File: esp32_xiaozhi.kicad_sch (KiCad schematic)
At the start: 5 parts

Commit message: Update schematics, PCB, and project files
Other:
- sheet esp32_C6 ports: added none; removed EN, IO_12, IO_13
- sheet max98357a ports: added none; removed GAIN, SD
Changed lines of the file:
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@@
-	(wire
-		(pts
-			(xy 168.91 107.95) (xy 177.8 107.95)
-		)
-		(stroke
-			(width 0)
-			(type default)
-		)
-	)
 	(wire
 		(pts
@@
 	(wire
 		(pts
-			(xy 220.98 105.41) (xy 232.41 105.41)
-		)
-		(stroke
-			(width 0)
-			(type default)
-		)
-	)
-	(wire
-		(pts
 			(xy 204.47 193.04) (xy 210.82 193.04)
 		)
@@
 		(pts
 			(xy 299.085 71.12) (xy 304.8 71.12)
-		)
-		(stroke
-			(width 0)
-			(type default)
-		)
-	)
-	(wire
-		(pts
-			(xy 220.98 107.95) (xy 237.49 107.95)
 		)
 		(stroke
@@
 		)
 	)
-	(label "IO_12"
-		(at 232.41 105.41 0)
-		(effects
-			(font
-				(size 1.27 1.27)
-			)
-			(justify left bottom)
-		)
-	)
 	(label "IO_11"
 		(at 245.11 72.39 180)
@@
 		)
 	)
-	(label "IO_13"
-		(at 237.49 107.95 0)
-		(effects
-			(font
-				(size 1.27 1.27)
-			)
-			(justify left bottom)
-		)
-	)
 	(label "OE"
 		(at 238.76 59.69 0)
@@
 			)
 			(justify right bottom)
-		)
-	)
-	(label "EN"
-		(at 168.91 107.95 0)
-		(effects
-			(font
-				(size 1.27 1.27)
-			)
-			(justify left bottom)
 		)
 	)
@@
 			)
 		)
-		(pin "GAIN" input
-			(at 74.93 143.51 0)
-			(effects
-				(font
-					(size 1.27 1.27)
-				)
-				(justify right)
-			)
-		)
 		(pin "LRC" input
 			(at 74.93 124.46 0)
-			(effects
-				(font
-					(size 1.27 1.27)
-				)
-				(justify right)
-			)
-		)
-		(pin "SD" input
-			(at 74.93 132.08 0)
 			(effects
 				(font
@@
 			)
 		)
-		(pin "EN" input
-			(at 177.8 107.95 180)
-			(effects
-				(font
-					(size 1.27 1.27)
-				)
-				(justify left)
-			)
-		)
 		(pin "IO_0" input
 			(at 177.8 111.76 180)
@@
 			)
 		)
-		(pin "IO_12" input
-			(at 220.98 105.41 0)
-			(effects
-				(font
-					(size 1.27 1.27)
-				)
-				(justify right)
-			)
-		)
-		(pin "IO_13" input
-			(at 220.98 107.95 0)
-			(effects
-				(font
-					(size 1.27 1.27)
-				)
-				(justify right)
-			)
-		)

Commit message: Add PWR_FLAG symbols to all schematic sheets to fix power_pin_not_driven ERC errors
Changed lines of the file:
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@@
 	)
 	(embedded_fonts no)
+	(symbol
+		(lib_id "power:PWR_FLAG")
+		(at 105.41 195.0 0)
+		(unit 1)
+		(body_style 1)
+		(exclude_from_sim no)
+		(in_bom no)
+		(on_board yes)
+		(in_pos_files no)
+		(dnp no)
+		(property "Reference" "#FLG007"
+			(at 105.41 190.0 0)
+			(hide yes)
+			(show_name no)
+			(do_not_autoplace no)
+			(effects
+				(font
+					(size 1.27 1.27)
+				)
+			)
+		)
+		(property "Value" "PWR_FLAG"
+			(at 105.41 200.0 0)
+			(hide yes)
+			(show_name no)
+			(do_not_autoplace no)
+			(effects
+				(font
+					(size 1.27 1.27)
+				)
+			)
+		)
+		(pin "1"
+			(uuid "a1b2c3d4-e5f6-7890-abcd-ef1234567890-pin1")
+		)
+		(instances
+			(project "esp32_xiaozhi"
+				(path "/cae338e8-f342-43cb-b99a-a0486629133c"
+					(reference "#FLG007")
+					(unit 1)
+				)
+			)
+		)
+	)
 )

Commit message: Revert PWR_FLAG additions - remove '??' squares from schematics
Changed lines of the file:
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@@
 	)
 	(embedded_fonts no)
-	(symbol
-		(lib_id "power:PWR_FLAG")
-		(at 105.41 195.0 0)
-		(unit 1)
-		(body_style 1)
-		(exclude_from_sim no)
-		(in_bom no)
-		(on_board yes)
-		(in_pos_files no)
-		(dnp no)
-		(property "Reference" "#FLG007"
-			(at 105.41 190.0 0)
-			(hide yes)
-			(show_name no)
-			(do_not_autoplace no)
-			(effects
-				(font
-					(size 1.27 1.27)
-				)
-			)
-		)
-		(property "Value" "PWR_FLAG"
-			(at 105.41 200.0 0)
-			(hide yes)
-			(show_name no)
-			(do_not_autoplace no)
-			(effects
-				(font
-					(size 1.27 1.27)
-				)
-			)
-		)
-		(pin "1"
-			(uuid "a1b2c3d4-e5f6-7890-abcd-ef1234567890-pin1")
-		)
-		(instances
-			(project "esp32_xiaozhi"
-				(path "/cae338e8-f342-43cb-b99a-a0486629133c"
-					(reference "#FLG007")
-					(unit 1)
-				)
-			)
-		)
-	)
 )

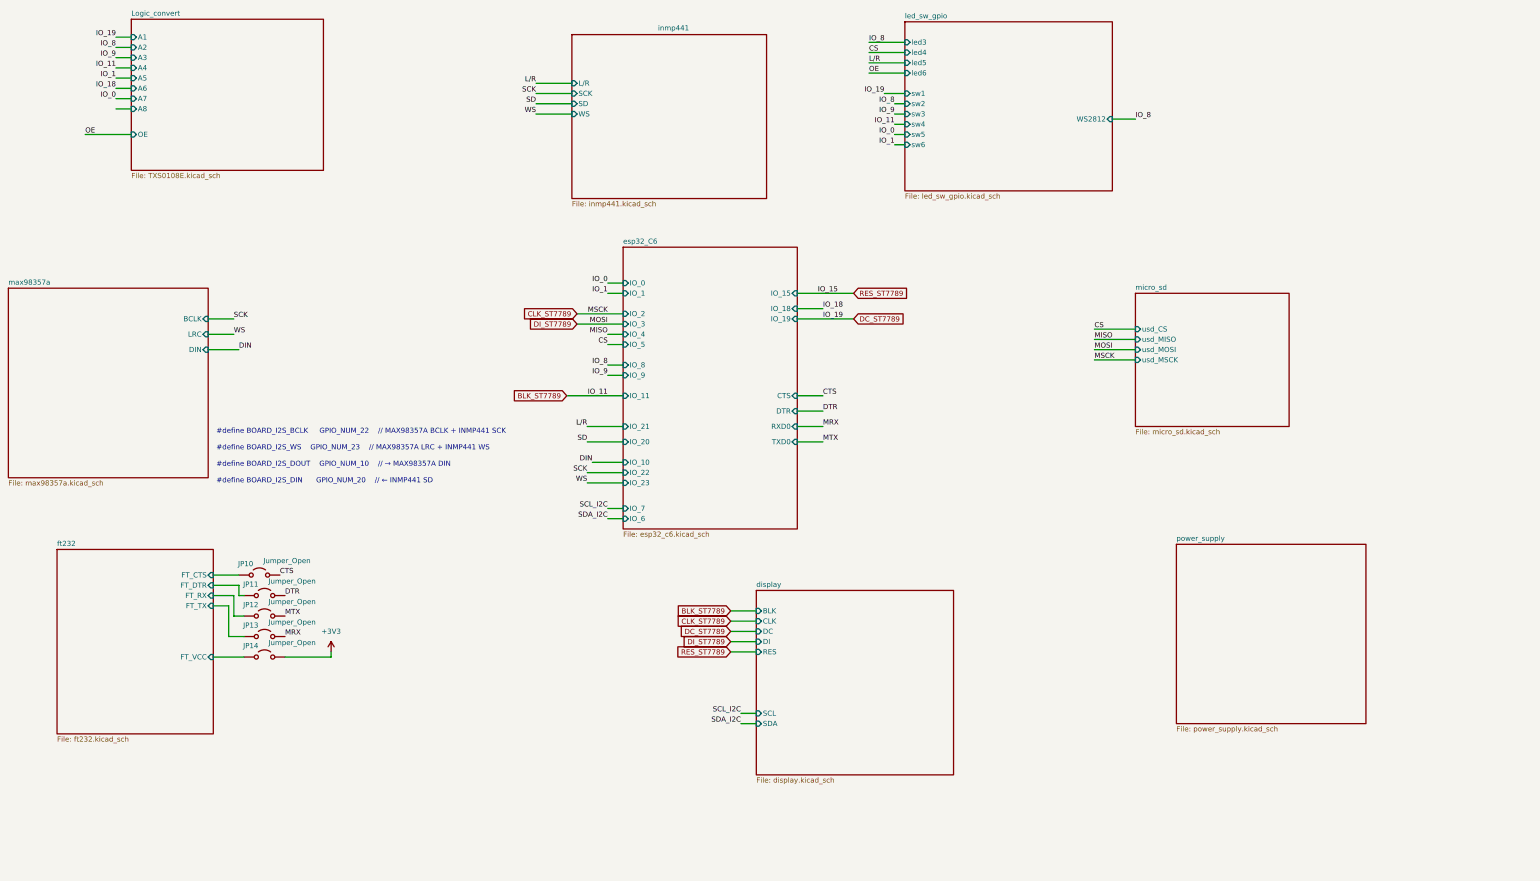
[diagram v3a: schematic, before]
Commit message: Actualización de esquema y PCB del proyecto ESP32C6 Xiaozhi
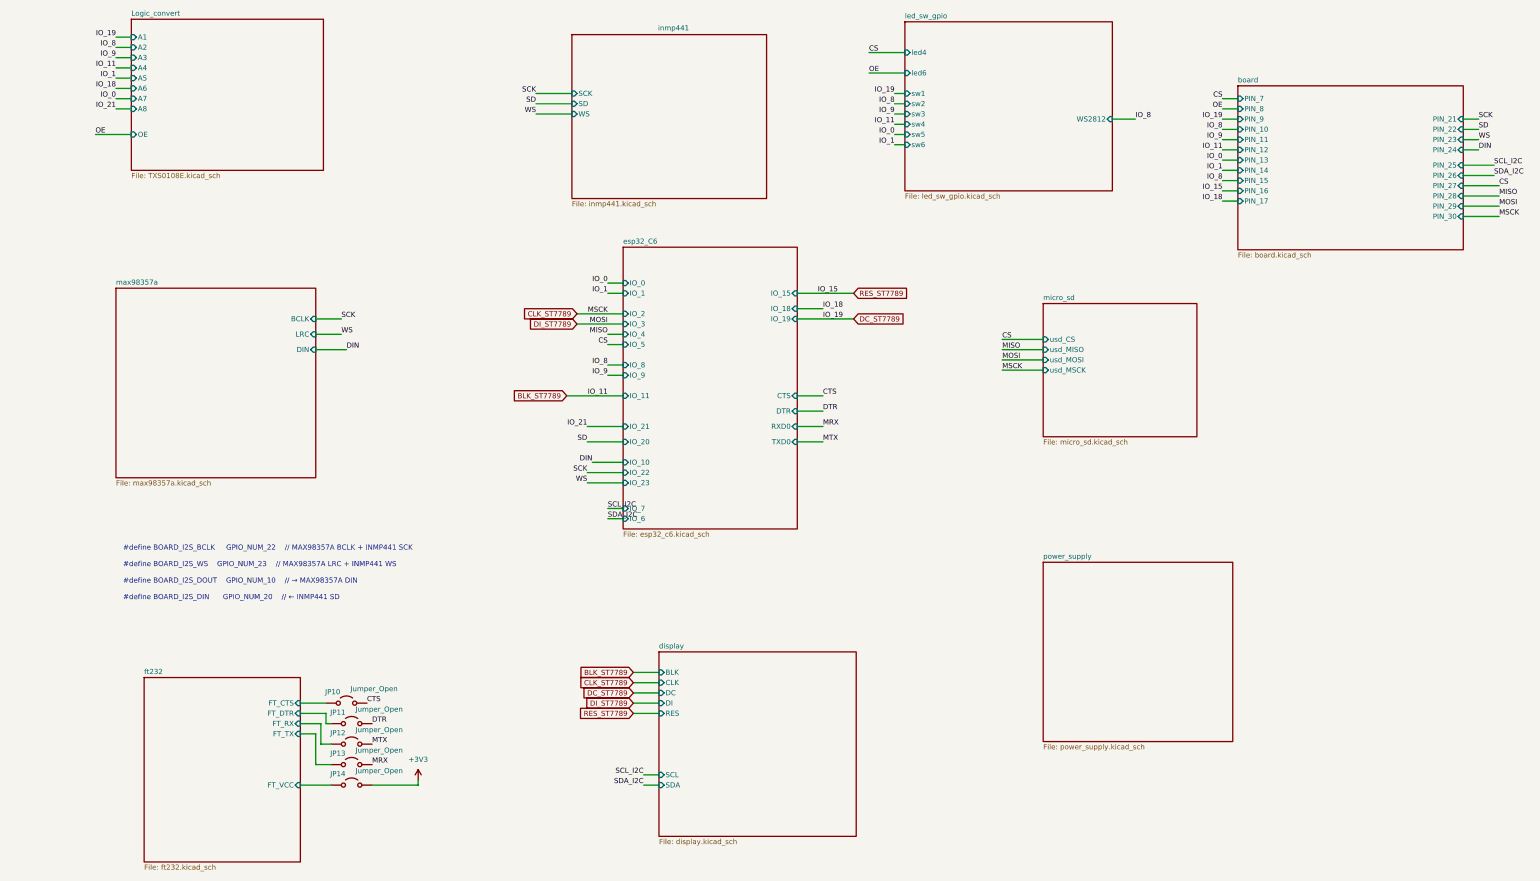
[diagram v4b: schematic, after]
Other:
- added sheet board (board.kicad_sch)
- sheet inmp441 ports: added none; removed L/R
- sheet led_sw_gpio ports: added none; removed led3, led5
- moved on the sheet: JP10, JP11, JP12, JP13, JP14

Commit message: Actualizaciones para versión single ESP32C6
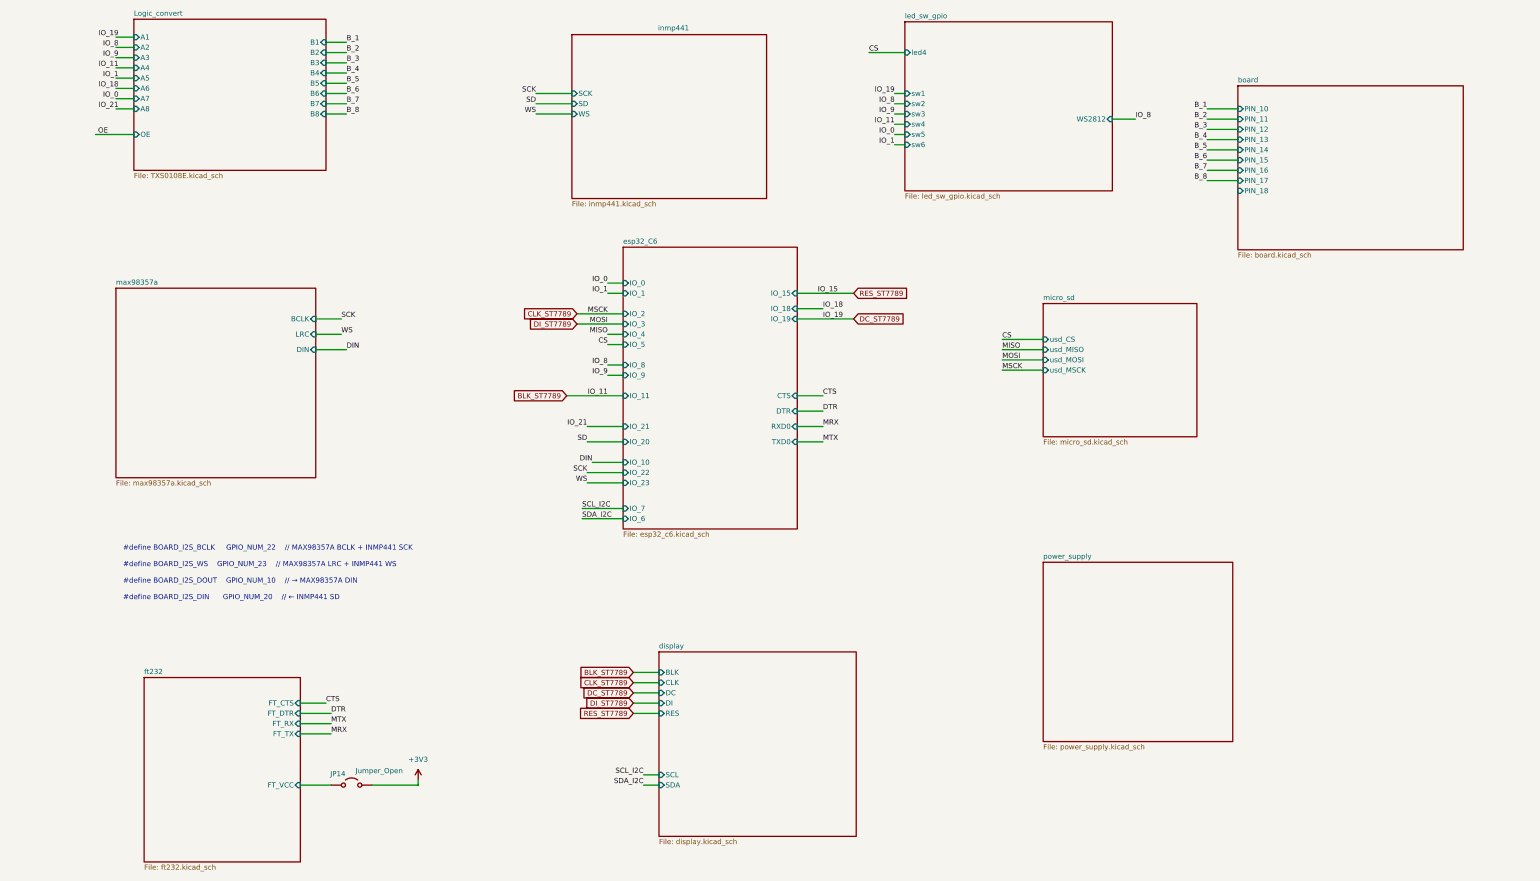
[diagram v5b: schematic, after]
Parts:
- removed JP10, JP11, JP12, JP13: Jumper_Open, Jumper:SolderJumper-2_P1.3mm_Open_RoundedPad1.0x1.5mm, symbol Jumper:Jumper_2_Open
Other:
- sheet Logic_convert ports: added B1, B2, B3, B4, B5, B6, B7, B8; removed none
- sheet board ports: added PIN_18; removed PIN_21, PIN_22, PIN_23, PIN_24, PIN_25, PIN_26, PIN_27, PIN_28, PIN_29, PIN_30, PIN_7, PIN_8, PIN_9
- sheet led_sw_gpio ports: added none; removed led6

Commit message: SCH: Update main schematic
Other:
- removed sheet board

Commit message: Actualización de esquemas y PCB con datos LCSC y librerías JLC
- Añade propiedades LCSC a los símbolos de las hojas de esquema
- Actualiza las hojas TXS0108E, display, esp32_c6, ft232, inmp441,
  led_sw_gpio, max98357a, micro_sd, power_supply y el esquema raíz
- Reorganiza el PCB (footprints, jumpers y nets) y actualiza el proyecto
- Incluye las librerías locales JLCImport (símbolos, huellas y modelos 3D)
  y las entradas correspondientes en fp-lib-table y sym-lib-table
- Añade la documentación técnica en docs/ y el archivo de posiciones
  esp32_xiaozhi-all.pos
- Elimina los ZIP generados gebers.zip y production.zip
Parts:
- JP14: now left out of the parts list
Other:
- sheet Logic_convert ports: added none; removed A1, A2, A3, A4, A5, A6, A7, A8, B1, B2, B3, B4, B5, B6, B7, B8, OE

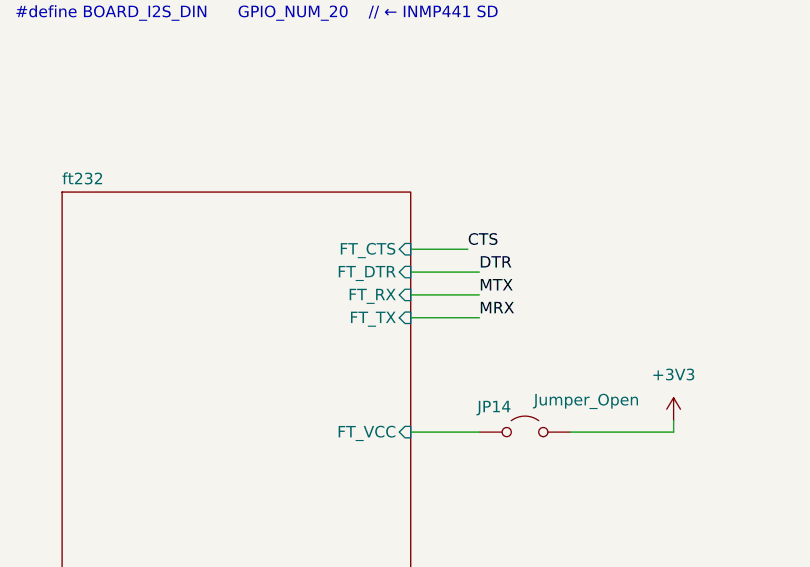
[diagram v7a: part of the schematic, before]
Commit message: adptador de ft232bm
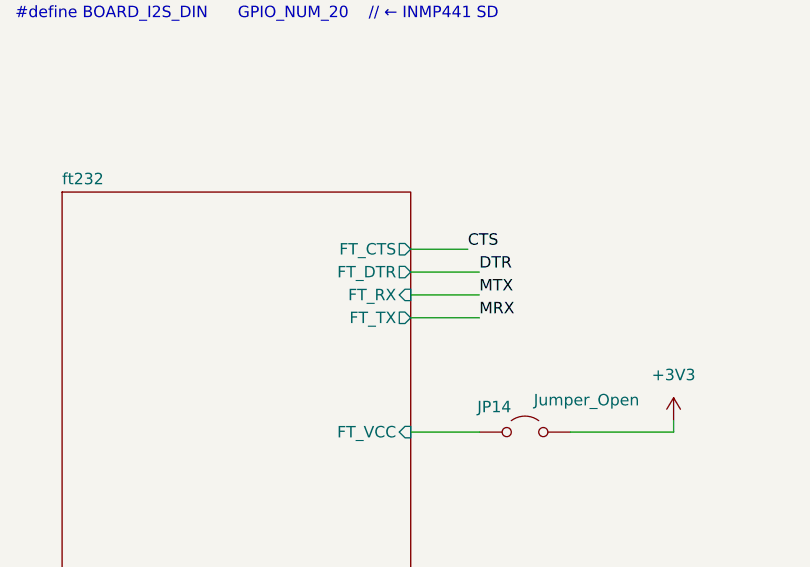
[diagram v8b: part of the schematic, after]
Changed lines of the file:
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@@
 			)
 		)
-		(pin "FT_CTS" input
+		(pin "FT_CTS" output
 			(at 97.79 215.9 0)
 			(effects
@@
 			)
 		)
-		(pin "FT_DTR" input
+		(pin "FT_DTR" output
 			(at 97.79 218.44 0)
 			(effects
@@
 			)
 		)
-		(pin "FT_TX" input
+		(pin "FT_TX" output
 			(at 97.79 223.52 0)
 			(effects
